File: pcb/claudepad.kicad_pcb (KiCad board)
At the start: 2 copper layers, 98 x 50 mm, 35 parts, among them SW1 ChocV2, SW10 ChocV2, SW11 ChocV2, SW12 ChocV2, SW13 ChocV2, SW14 ChocV2, SW2 ChocV2, SW3 ChocV2, SW4 ChocV2, SW5 ChocV2, SW6 ChocV2, SW7 ChocV2, SW8 ChocV2, SW9 ChocV2

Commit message: PCB 第二版：主控排针改 1×13（实物 13 脚）+ USB 开孔从右壁挪到上壁
第一版已报废，两个硬伤：

【1】主控排针 12 孔 → 13 孔（致命）
  实物每排 13 个引脚、跨距 30.48mm（= 12 × 2.54）。原按 KiCad 1x12 封装生成
  （跨距 27.94），于是 12 个孔相对 13 个引脚**每个都偏 1.27mm（半个间距）**，
  还少一个孔 —— 主控根本插不上去。
  根因：params.scad 里写着「30.48 引脚跨度」却没记「一排几个脚」，
  生成器只能自己写死孔数，全项目没有一处校验这个数。
  三重独立核实：① 官方尺寸图像素标定 13 个焊盘、间距 2.54、跨距 30.50（板框长宽
  比 1.855 对上 33.00/17.78）；② 官方引脚图每列 13 个信号名；③ 实物照片 USB 壳
  压住列首 3 个 + 可见 10 个 = 13。

【2】USB 开孔开在右壁（错墙）
  USB-C 在 17.78mm 的**短边**上（沿 33mm 长轴）；本设计主控长轴沿 y → USB 朝 +y。
  原 case_bottom.scad 的 usb_cutout() 开在右壁，位置和朝向都不对。
  连带更正：2026-09-16「PCB 加宽 86→98 解决 USB 够不到右壁」是在解决不存在的问题。

改动
- tools/gen_kicad.py：PinHeader_1x13；MCU_PAD_Y1 42.97→45.74；JP1/JP2 net 表重排为
  13 项（左排 GND D1 D0 GND GND D2 D3 D4..D9；右排 B+ RAW GND RST VCC D21 D20 D19
  D18 D15 D14 D16 D10）；新增自检「孔数与跨距 == 实物引脚」；丝印改 USB -> +Y WALL
- cad/lib/params.scad：新增 NANO_PIN_COUNT/PITCH/SPAN、USB_PORT_W/H/R；
  NANO_POS_Y 8.50→14.00；更正「USB 朝右壁」的注释
- cad/case_bottom.scad：usb_cutout() → usb_port()，开在 +y 上壁、中心对准主控短边
  中点；孔按插头胶壳开（11×8）而非金属头 —— 插座距壁 11.3mm 而插头金属仅 6.5mm，
  肩部必须伸进内腔 4.5mm，而壁厚只有 2.4mm 做不出这么深的沉台
- tools/gen_pcb.py：netlist.json 新增 mcu 块（引脚数/间距/跨距/位置），供 gen_kicad 断言
- docs/焊接指南.md：排针表 12 行→13 行，附「怎么认 pad1」
- docs/打样下单指南.md：24 孔→26 孔；顶部标注第一版作废、第二版待布线出 Gerber

校验：DRC 0 错误（59 未连接=布线前预期）；check_dims / lint_scad / verify_geometry /
check_keymap / export_stl / verify_stl / gen_viewer / draw_travel / test_hook 全通过；
USB 开孔位置用 STL 实体点测试验证（孔中心空、四周实、旧右壁位置已实心）
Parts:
- JP1, JP2: footprint PinHeader_1x12_P2.54mm_Vertical -> PinHeader_1x13_P2.54mm_Vertical
- moved JP1 2.77 mm to (81.0, 4.26)
- moved JP2 2.77 mm to (96.2, 4.26)
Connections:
- JP1 pad 1: (no net) -> GND
- JP1 pad 10: COL1 -> ROW3
- JP1 pad 11: COL2 -> COL1
- JP1 pad 12: COL3 -> COL2
- JP1 pad 3: GND -> (no net)
- JP1 pad 5: (no net) -> GND
- JP1 pad 7: ROW1 -> (no net)
- JP1 pad 8: ROW2 -> ROW1
- JP1 pad 9: ROW3 -> ROW2
- JP2 pad 10: COL6 -> RGB_DIN
- JP2 pad 11: COL5 -> COL6
- JP2 pad 12: COL4 -> COL5
- JP2 pad 2: GND -> (no net)
- JP2 pad 3: RST -> GND
- JP2 pad 4: (no net) -> RST
- JP2 pad 9: RGB_DIN -> (no net)
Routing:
- net ROW1: track 148.3 -> 0.00 mm
- net COL1: track 142.1 -> 0.00 mm
- net ROW2: track 137.4 -> 0.00 mm
- net ROW3: track 128.4 -> 0.00 mm
- net COL2: track 93.4 -> 0.00 mm
- net COL3: track 91.5 -> 0.00 mm
- net COL4: track 81.8 -> 0.00 mm
- net COL5: track 75.3 -> 0.00 mm
- net GND: track 38.4 -> 0.00 mm
- net RST: track 38.2 -> 0.00 mm, vias 2 -> 0
- net COL6: track 26.8 -> 0.00 mm
- net RGB_DIN: track 20.9 -> 0.00 mm
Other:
- board text added: "USB -> +Y WALL (top)"
- board text removed: "USB -> RIGHT WALL"

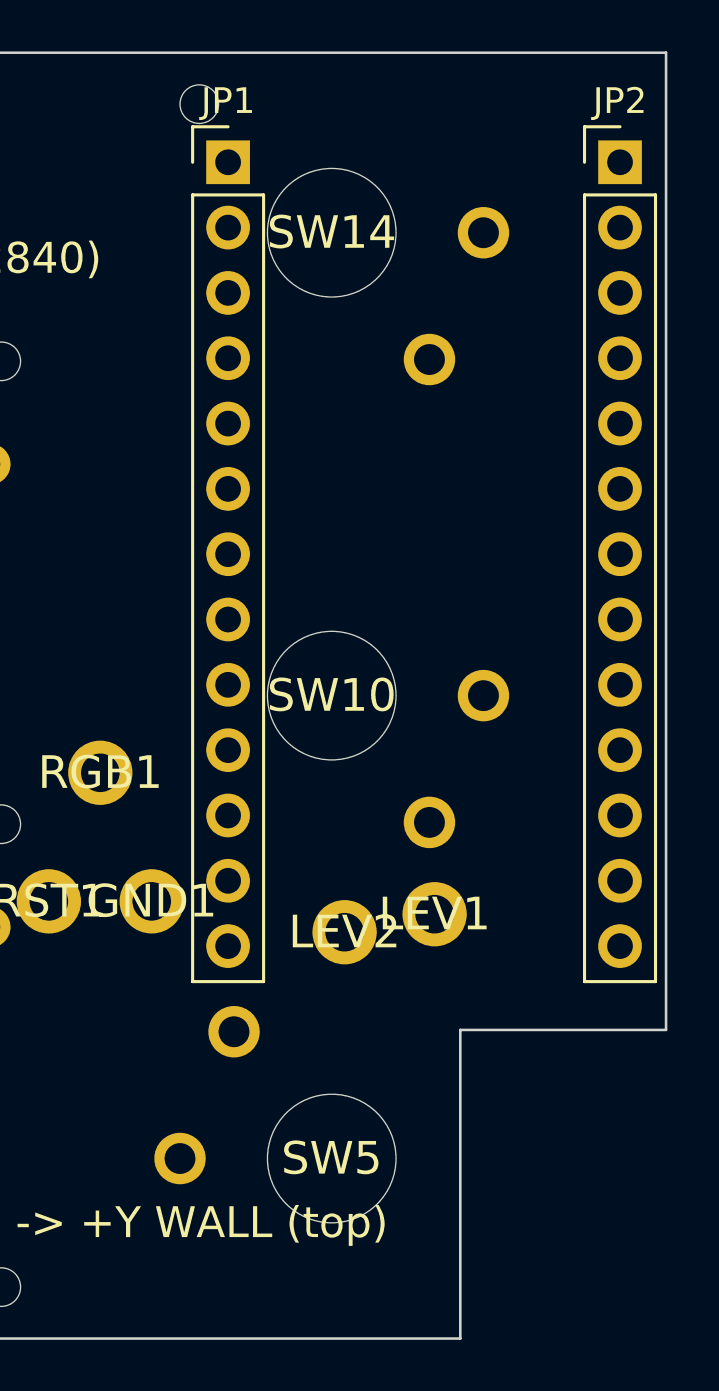
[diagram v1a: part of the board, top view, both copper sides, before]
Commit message: 轴体定位脚孔：STOP 靠旋转补齐 4 孔；ENTER(2) 判定几何无解需剪脚
用户发现：右列中间那颗轴体（回车第2轴）只有 2 个引脚孔、没有定位脚孔，
少一条腿根本装不进去。核实属实 —— 原设计 NPTH_SKIP 省掉了 ENTER(1) 与 STOP(0)
两个定位孔。

逐角度穷举（4 个旋转角 × 4 个轴体特征 × 与全板每个孔的实际净距）：

- STOP(85,7)：270° 时 4 个孔全部成立 ✓
  电气脚1 (89.93,10.80) 需缺口上缘收窄 → PCB_NOTCH_Y1 12.00→9.00
  （缺口仍完整容纳拨杆本体 y[2.4,8.8]，余 0.2mm）
- ENTER(2)(85,25)：**几何无解** —— 四个角各有一条腿不成立：
    0°/90°  电气脚撞左排孔（差 0.5mm 以上）
    90°/270° 定位脚撞左排孔
    180°    定位脚 (79.85,30.00) 距左排最近孔 1.23 < 1.95
  根因：轴体中心 x=85 与主控左排 x=80.97 只差 4.03mm，而 Choc 的脚伸到 ±5.90mm；
  同时主控两排固定 15.24 间距、轴体壳宽 13.95，在 98mm 板宽内无法同时避开
  「两排孔」和「两个轴体壳」（我算过：需要 JP1≤77.05 且 JP2≥92.95，
  但 JP2−JP1 必须 =15.24，矛盾 0.66mm）
  → 保留省孔，改为装配时剪掉该定位脚（已写入焊接指南）

- VOICE(85,43)：定位脚 (79.85,48.00) 本就在主控区外 ✓ 不动
- 轴体 pad 数 54 → 55（只省 1 个孔）

顺带修掉一个会漂移的副本
- 轴体旋转角原先在 gen_pcb.py 与 gen_kicad.py 各硬拷贝一份（注释写着「需两处同步」）
  → 改为写进 netlist.json 的 switch_rot，gen_kicad.py 只读不算
- gen_kicad 自检「NPTH 在主控区」由错误降为警告（孔必须打，靠主控垫高解决高度）

另外发现一个装配死锁并已修正文档
- 原顺序「② 排针+主控 → ④ 轴体」会锁死：那 4 个轴体脚在主控正下方，装上主控就
  焊不到。正确顺序是先焊轴体（背面），最后装主控 —— 主控的焊点在它自己朝下的
  焊盘那面，最后从下面焊，全程可达 ✓

校验：DRC 0 错误；9 项脚本全过
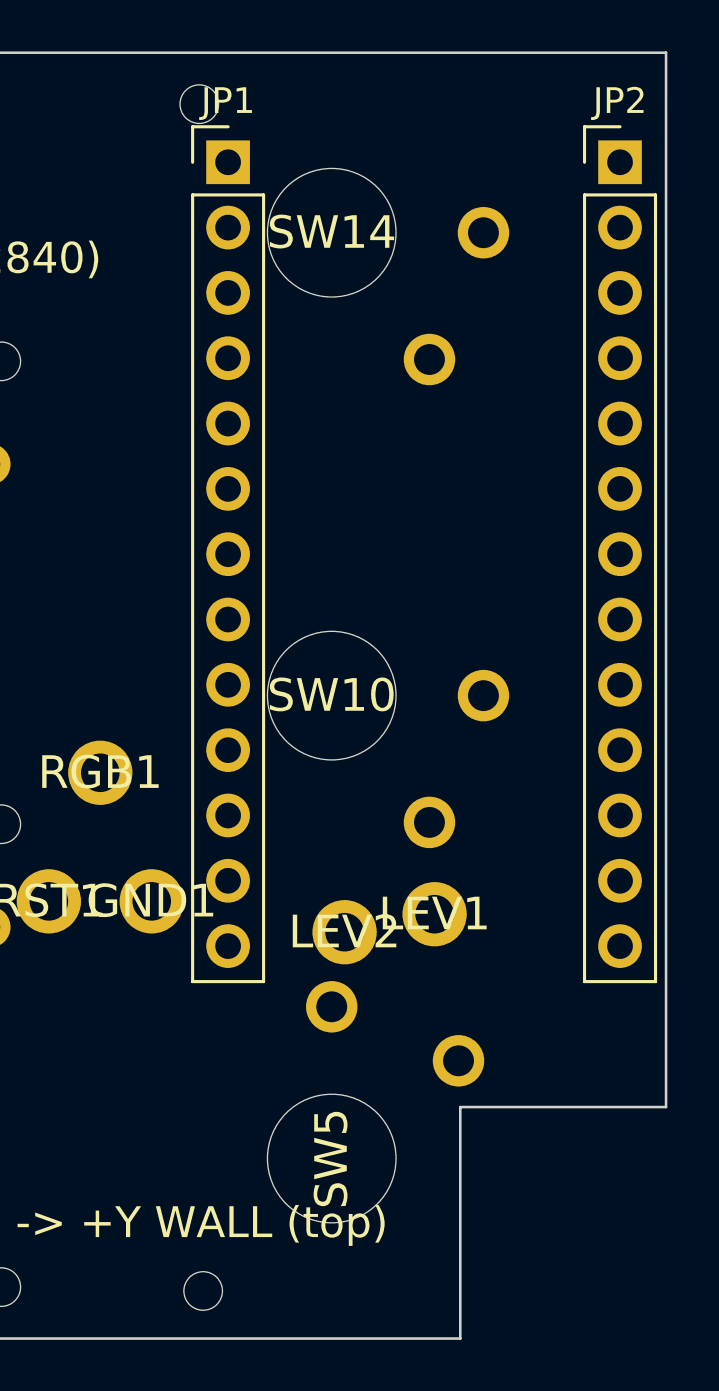
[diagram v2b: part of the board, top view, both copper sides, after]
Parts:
- turned SW5 to -90 degrees
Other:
- outline, holes or cut-outs redrawn

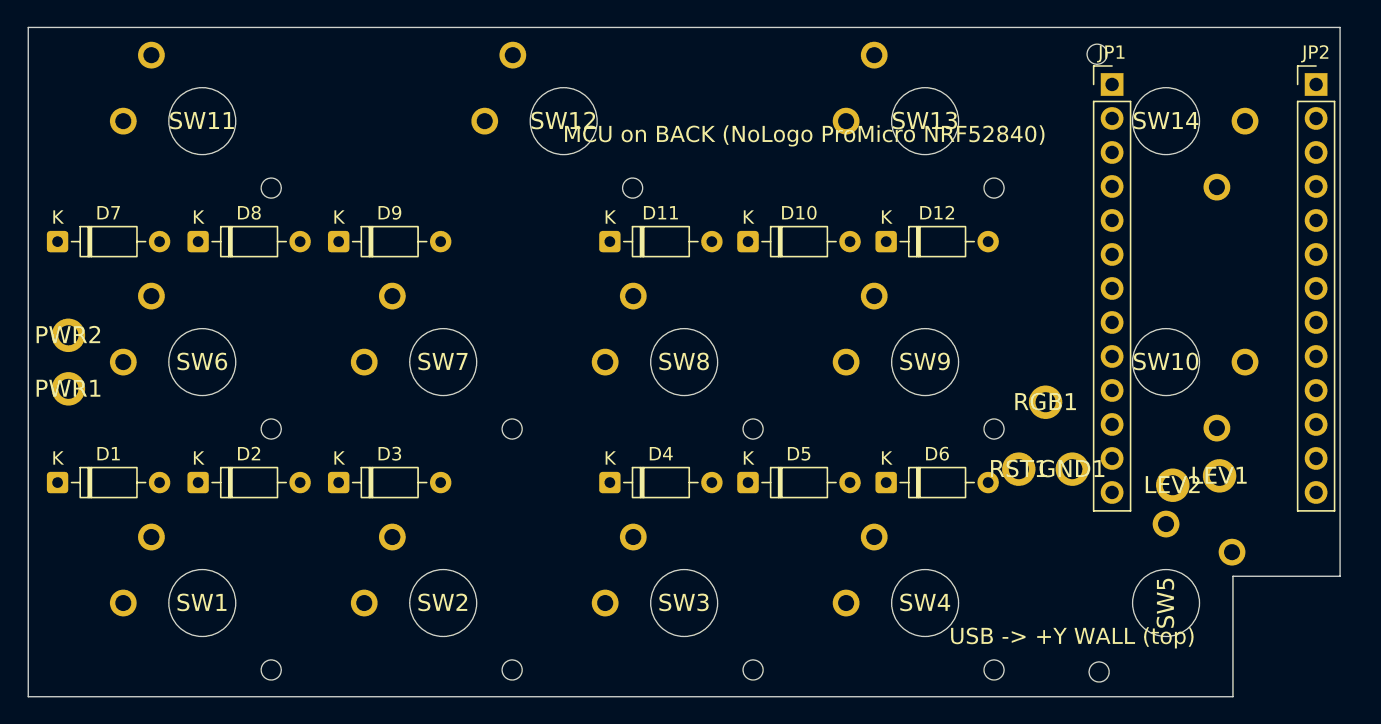
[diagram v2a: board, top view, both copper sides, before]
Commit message: ★ 14 颗轴体全部补齐 4 孔：板宽 98→99 + 主控位置重新解算
承接上一笔：上一笔判定「回车(2) 的定位脚几何无解，装配时剪脚」。用户提出
「让两条腿和另一条腿分居排针两侧」——顺着这个思路重算，发现不是无解，
只差 0.9mm，而这点位移可以靠**加宽板子 1mm** 换出来。

改动
- PCB_W 98 → 99，PCB_X 写死 2.0（不再按居中算：定位板轴孔在板坐标 15/33/…/87，
  PCB 轴体在 13/31/…/85，必须 PCB_X + 13 = 15。PCB_X 一变整机就装不上）
- PCB_NOTCH_D 8 → 9（板加宽后同步 +1，使缺口内缘**绝对位置不变**，仍在板坐标 x=90）
- 主控位置**解出来的**（穷举 0.01mm 步长取最小余量最大者）：
  NANO_POS_X 79.70→80.11、NANO_POS_Y 14.00→12.26
  左排孔 80.97→81.38、右排 96.21→96.62、pad1 y 45.74→44.00
  四条约束（回车(2)定位脚≥1.85、回车(2)中心孔≥3.60、语音中心孔≥3.60、
  语音定位脚≥1.85，均按「孔边缘↔对方铜皮」算）最小余量 **0.119mm** ✓
  ⚠️ 关键点：2.54 的孔栅格必须与 25.0/43.0 两个 Ø5 中心孔错开半格，
  否则最近孔正对中心孔，怎么挪 x 都不够
- NPTH_SKIP 清空 → **14 颗轴体 × 4 孔 = 56 孔，一条腿都不用剪**
- 焊接指南：删掉「回车第2轴剪定位脚」（已不成立），保留「轴体先焊、主控最后装」

顺带修掉两处**重复计算**（同一类 bug，都是「量恰好相等时看不出来」）
- tools/gen_pcb.py：自己又算了一遍 (PLATE_W−PCB_W)/2 而不读 params 的 PCB_X
  → 板加宽后 1.5 vs 2.0 分叉，所有轴体 PCB 坐标整体漂 0.5mm
- tools/check_dims.py：同一处重复计算 → 误报「支撑台不在间隙中心」
  两处都改为只读 params

校验：DRC 0 错误（56 个轴体孔全部保留）；check_dims 29/29、lint_scad、verify_geometry、
check_keymap、export_stl、verify_stl、gen_viewer、draw_travel、test_hook 全过；
渲染层（步骤图/参考图/裸板渲染）全部重生成
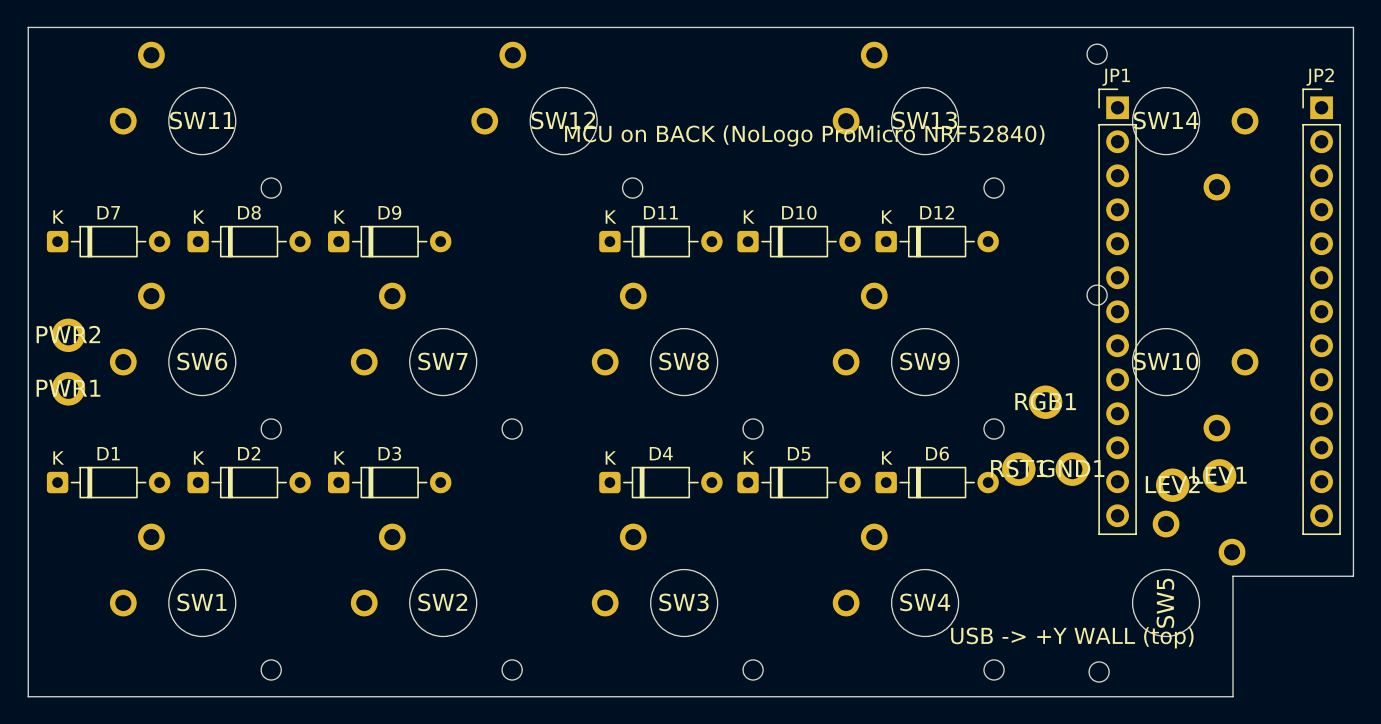
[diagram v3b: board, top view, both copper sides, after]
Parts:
- moved JP2 1.79 mm to (96.6, 6.00)
- moved JP1 1.79 mm to (81.4, 6.00)
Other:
- board size 98 x 50 mm -> 99 x 50 mm

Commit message: 布局改版：空格跨列 1-4 → 2-4（3u）+ 回车(2) 转 90° 孔竖着 + 主控重新解算
按用户要求改的三件事：

【1】空格那一行紧凑对齐
  KEYMAP 的 [1,3,4,SPACE] → [2,3,3,SPACE]。3 根轴从 13/40/67（间距 27）变成
  31/49/67（间距 18），与上面两行的列对齐，行内不再有大空档，最左一列空出。
  连带：键帽 4u(71.6mm) → 3u(53.6mm)；keycap.scad 的 keycap_mode 增加 3u、去掉 4u；
  export_stl 输出 05_keycap_3u.stl（旧的 4u STL 已删）

【2】回车(2) 转 90°，孔竖着
  SWITCH_ROT 的 (ENTER,1) 由 180 改 90。它的定位脚随之落到 (90.00,30.15)、
  电气脚落到 (80.07,21.20) —— 后者要求主控左排孔从 81.38 挪到 78.03，
  而左移会被 x=76 的支撑台挡住 → 支撑台 X2 由 76 改到 58（同为列间隙中心）
  主控左移后压住复位/RGB 三个飞线焊盘 → PAD_GND (78,17)→(74,13)、
  PAD_D15 (76,22)→(75.5,22)

【3】主控位置重新解算（不是手调）
  把 14 颗轴体 56 个孔 + 支撑台 + 板缘 + 缺口一起列为约束，穷举 0.01mm：
  左排 78.03 / 右排 93.27 / pad1 y=45.30，主控本体 x[76.76,94.54] y[13.56,46.56]
  最小余量 0.682mm（比上一版的 0.119mm 宽裕得多）
  注：排针孔按「孔边缘 ↔ 对方铜皮」算，且 pad1 是方盘（有效半径 1.20 不是 0.85）

校验：DRC 0 错误；check_dims 29/29、lint_scad、verify_geometry、check_keymap、
verify_stl、export_stl、gen_viewer、draw_travel、test_hook 全过

修掉四处会撒谎的展示层（都是 4u 空格时代的硬拷贝）
- tools/verify_stl.py：期望清单还写着 05_keycap_4u.stl，而它只遍历目录里实际存在的
  文件，所以改名后静默跳过、照样报「全部通过」。已改为 3u 并新增反向检查（清单里的
  文件必须都在）；用改名做了变异测试，确认它现在真的会报错
- tools/view_model.py、cad/output/viewer.html(CAP_FILES)、cad/pcb_assembly.scad、
  tools/render_assembly.py：写死的旧空格坐标(13/40/67)与旧文件名
- tools/render_assembly.py：删掉「STOP、ENTER 第二轴没有定位孔属正常」这句（已不成立）
- 新增 docs/img/board-annotated.png（带标注对照图）
      docs/img/space-row-before-after.png（空格改前/改后示意）
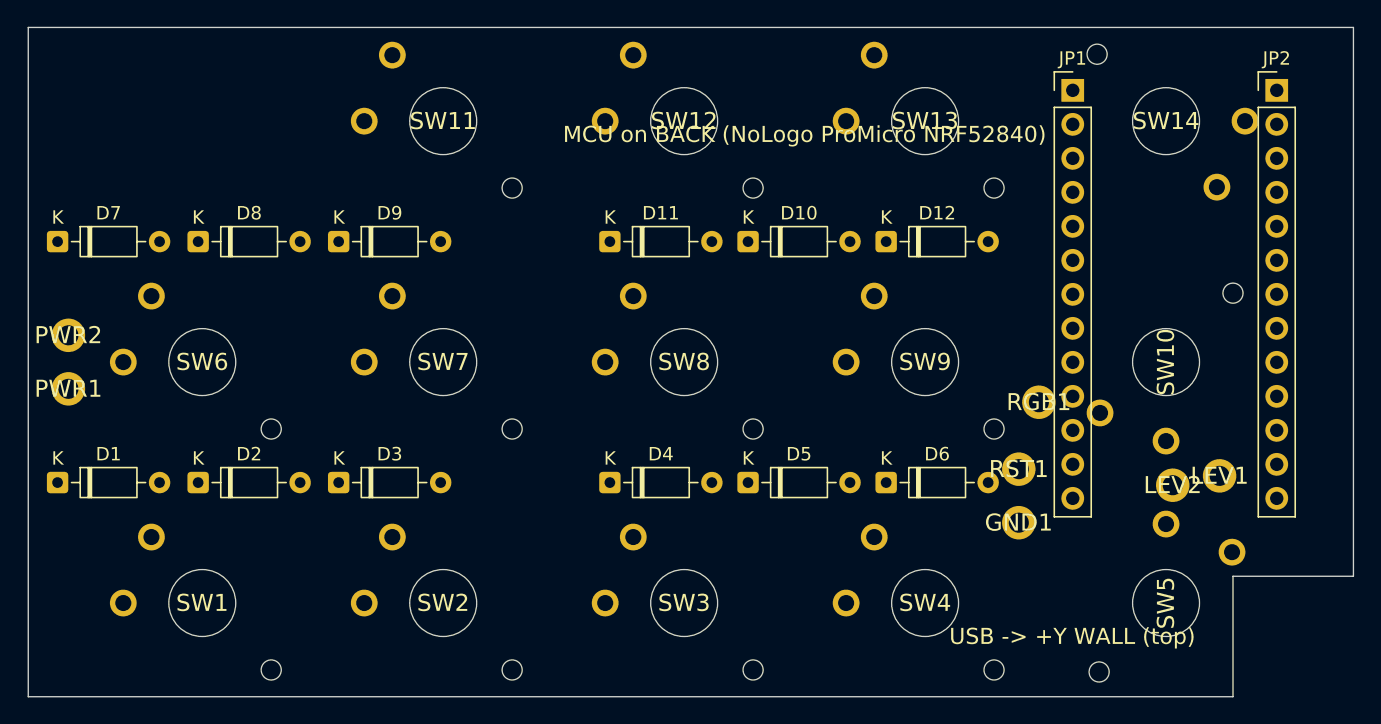
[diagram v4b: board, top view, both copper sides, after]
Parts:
- moved SW11 18.0 mm to (31.0, 7.00)
- moved SW12 9.00 mm to (49.0, 7.00)
- moved GND1 5.66 mm to (74.0, 37.0)
- moved JP2 3.59 mm to (93.3, 4.70)
- moved JP1 3.59 mm to (78.0, 4.70)
- moved RGB1 0.50 mm to (75.5, 28.0)
- turned SW10 to 90 degrees
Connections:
- D11 pad 2: COL1 -> COL2
- SW11 pad 1: COL1 -> COL2
- SW12 pad 1: COL1 -> COL2
- SW13 pad 1: COL1 -> COL2

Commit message: 布局再改：空格那行 4 颗键贴左排（跨列 1-3 + 语音列 4）+ 定位板切孔 bug 修复
用户原话（2026-10-11）：'最下层不是有四个键而已吗？我们之间给他并排与上方对其'
+ 澄清 '第 1~4 列，最左列不该空出来'。上一版误改成跨列 2-4 + 最左列空出，方向反了。

【1】空格行贴左
  KEYMAP [2,3,3,SPACE] + [5,3,1,VOICE] → [1,3,3,SPACE] + [4,3,1,VOICE]
  空格 3 轴 31/49/67 → 13/31/49（全部落在 18mm 网格线上）；语音键列 5 → 列 4
  列 5（x=85）空出 → 主控上方不再压任何轴体（原 VOICE 正好压在主控上）
  连带：overlay 矩阵变换末行 RC(2,4) → RC(2,3)；空格 net COL2 → COL1

【2】★ 定位板切孔 bug（渲染预览时发现）
  choc_cutout() 用 linear_extrude(center=true) 又被 translate z=-1，
  切槽只覆盖 z[-2.6,0.6]，而板厚 [0,1.2] → 顶面留 0.6mm 皮没切穿。
  STL 体积 6.33 cm³（实心板 + 4 螺丝孔）→ 修后 4.61 cm³。
  也就是说：**之前导出的定位板 STL 轴体根本插不进去**。

【3】展示层修漂移（都是会撒谎的硬拷贝）
  · tools/render_assembly.py：写死的板宽 98 / JP 80.97 / NANO 79.70 / 空格 31-49-67
    → 全改为读 pcb/placement.csv + 板文件 + params；俯视图孔位改为按真实旋转角算
    （原先只做 180° 镜像，STOP 270° / ENTER 90° 的孔画错位置）
  · cad/pcb_assembly.scad：SWITCHES / JP_XS / JP_N / 主控位置与 USB 朝向 / 复位焊盘
  · tools/check_dims.py：空格挠度按 4u 算 → 从 KEYMAP 推导（3u：单轴 0.67 / 三轴 0.08）
  · 新增 tools/render_board_annotated.py：board-annotated.png 等改由脚本生成

【4】重生成产物
  pcb/claudepad.kicad_pcb（99×50）· pcb/steps/*（6 个）· placement.csv / netlist / wiring
  cad/output/*.stl（6 个，含修好的定位板）· docs/img/*（板子 5 视角 + 分步 8 张 +
  焊接参考图 + 标注图 + 顶视预览）· pcb/claudepad_render.kicad_pcb（含 3D 模型）

【5】文档同步：焊接指南 / PCB 规格书 / 打样下单指南 / 改板方案 / PRD / 结构 / 采购 /
  项目报告 / README / firmware README / MEMORY.md（4u→3u、98→99、排针列位、主控坐标）

校验：check_dims 29/29 · lint_scad · verify_geometry · check_keymap · verify_stl ·
test_hook 全过；DRC 0 错误（39 条丝印警告 + 59 未连接，未布线预期）
⚠️ 尚未布线、未出 Gerber（打样前必须补）
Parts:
- moved SW11 18.0 mm to (13.0, 7.00)
- moved SW12 18.0 mm to (31.0, 7.00)
- moved SW13 18.0 mm to (49.0, 7.00)
- moved SW14 18.0 mm to (67.0, 7.00)
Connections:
- D11 pad 2: COL2 -> COL1
- D12 pad 2: COL5 -> COL4
- SW11 pad 1: COL2 -> COL1
- SW12 pad 1: COL2 -> COL1
- SW13 pad 1: COL2 -> COL1
- SW14 pad 1: COL5 -> COL4

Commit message: 布线完成 + 修致命电路拓扑（二极管/轴体并联 → 串联）+ 出 Gerber
⚠️ 用户要求『去嘉立创下单』，但板子当时不能下单：没布线、Gerber 是第一版的。
   本次把前置条件全部做完了。

【1】★ 致命电路错误：二极管与轴体并联（发现于核对焊盘网络）
  SW1: pad1→COL1, pad2→ROW1 ／ D1: K→ROW1, A→COL1 —— 两者**并联**。
  后果：驱动任一列都会经二极管直接灌通行线 → 该列按键恒为『按下』，键盘不可用。
  正解（与 netlist.md 的『列 → 阳极 → 阴极 → 轴体 → 行』一致）是**串联**：
      列 COL ── A▷|── K ── MID ── 轴体pad1 ──[按下]── pad2 ── ROW
  · gen_pcb.py：每个矩阵位置新增局部网络 net_mid（大键多轴共用；拨杆用 APPROVE_MID）
  · gen_kicad.py：轴体 pad1→MID / pad2→ROW；二极管 K→MID / A→COL
  · gen_kicad.py 自检新增**串联断言**（几何检查查不出这类错，必须断言网络）
  · 第一版板子也带这个错（已作废，未流出）

【2】自动布线（打通链路）
  tools/export_dsn.py（新增）→ FreeRouting → tools/import_ses.py → 174 段 + 3 过孔
  · FreeRouting 原生 CLI v2.5.0 在本项目 DSN 上崩（GraalVM 序列化限制），
    改用 freerouting-1.9.0.jar + OpenJDK 21（1.7 秒布完）
  · tools/patch_route.py（新增）补自动布线漏掉的 ROW3 一段（绕开两个 Ø5 中心孔）
  · DRC：**0 错误 / 0 未连接**（39 条丝印警告为既有，不影响打样）

【3】出 Gerber（第二版打样包）
  pcb/fabrication/claudepad-jlc.zip —— 10 个文件（F/B 铜箔·阻焊·丝印 + 板框 + 钻孔 + 网表）
  第一版全套（含 9-28 的 zip）归档到 pcb/fabrication/v1-2026-09-28/，避免误下单

【4】文档
  · 打样下单指南：状态改为『可以下单』，补下单参数（建议勾飞针电测）与到货核对项
  · 焊接指南：二极管极性说明改为串联口径；★ 新增『列 ↔ 行 不导通』万用表检查
  · 全部『阳极接列、阴极接行』措辞改为『阳极朝列、阴极朝行（与轴体串联）』
  · MEMORY.md：新增布线/打样链路一节（含 FreeRouting 版本坑与镜像）

校验：check_dims 29/29 · lint_scad · verify_geometry · check_keymap · verify_stl ·
test_hook 全过；DRC 0 错误 / 0 未连接
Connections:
- D1 pad 1: ROW1 -> MID_R1C1
- D10 pad 1: ROW2 -> MID_R2C4
- D11 pad 1: ROW3 -> MID_R3C1
- D12 pad 1: ROW3 -> MID_R3C4
- D2 pad 1: ROW1 -> MID_R1C2
- D3 pad 1: ROW1 -> MID_R1C3
- D4 pad 1: ROW1 -> MID_R1C4
- D5 pad 1: ROW1 -> MID_R1C5
- D6 pad 1: ROW1 -> APPROVE_MID
- D7 pad 1: ROW2 -> MID_R2C1
- D8 pad 1: ROW2 -> MID_R2C2
- D9 pad 1: ROW2 -> MID_R2C3
- SW1 pad 1: COL1 -> MID_R1C1
- SW10 pad 1: COL4 -> MID_R2C4
- SW11 pad 1: COL1 -> MID_R3C1
- SW12 pad 1: COL1 -> MID_R3C1
- SW13 pad 1: COL1 -> MID_R3C1
- SW14 pad 1: COL4 -> MID_R3C4
- SW2 pad 1: COL2 -> MID_R1C2
- SW3 pad 1: COL3 -> MID_R1C3
- SW4 pad 1: COL4 -> MID_R1C4
- SW5 pad 1: COL5 -> MID_R1C5
- SW6 pad 1: COL1 -> MID_R2C1
- SW7 pad 1: COL2 -> MID_R2C2
- SW8 pad 1: COL3 -> MID_R2C3
- SW9 pad 1: COL4 -> MID_R2C4
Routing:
- net ROW1: track 0.00 -> 111.2 mm, vias 0 -> 1
- net ROW3: track 0.00 -> 102.0 mm
- net COL1: track 0.00 -> 101.0 mm
- net ROW2: track 0.00 -> 91.6 mm
- net COL2: track 0.00 -> 77.4 mm
- net COL3: track 0.00 -> 70.5 mm, vias 0 -> 1
- net COL4: track 0.00 -> 67.0 mm, vias 0 -> 1
- net GND: track 0.00 -> 56.9 mm
- net MID_R3C1: track 0.00 -> 52.1 mm
- net RST: track 0.00 -> 44.5 mm
- net MID_R2C4: track 0.00 -> 40.3 mm
- net MID_R1C5: track 0.00 -> 38.3 mm
- net COL5: track 0.00 -> 34.4 mm
- net APPROVE_MID: track 0.00 -> 30.0 mm
- net MID_R2C3: track 0.00 -> 23.7 mm
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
